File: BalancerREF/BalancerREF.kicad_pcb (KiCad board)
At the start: 4 copper layers, 50 x 50 mm, 79 parts, among them J1 USB4105-GF-A, J2 LiPo 500mAh PROTECTED, J3 MAG+ / MAG- PTH, J4 GPS MODULE 3V3 UART, J5 OPTICAL HEAD 7-WAY, Q4 AO3401A, SW1 POWER, SW2 ACQUIRE, SW3 BOOT / SERVICE, U1 ESP32-S3-MINI-1-N8, U10 SN74LVC1G123DCTR, U2 IIS3DWBTR, U3 LM1815MX/NOPB, U5 BQ24075RGT, U6 TPS63031DSKR, U7 SRV05-4MR6T1G, U9 SN74LVC1G132DBVR

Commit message: fix: BOM fields, silkscreen labels, +3V3 plane, and stale docs before review
- MPN fields: R3/R35/R36 (were "100k"), U9 (was the 1G08), R18 (was 3R0)
- Title block: HOBOVibe spelling; head company line no longer says "human
  review required"
- C20 on the head board rated 10 V; SYS_SW can sit at 5.5 V
- Silkscreen: board name and rev on both boards, battery and MAG polarity,
  pin-1 marks on J4 and both J5
- Main PCB: SYS, SYS_SW, BAT and USB_VBUS tracks removed from In2.Cu so the
  +3V3 plane is whole; three vias that only served them removed. Those four
  nets need re-routing on the outer layers.
- Docs: routing state, ground-pour wording, missing head-board holes,
  JLCPCB parts table rebuilt for the Rev F BOM, superseded LIS2DW12 and
  phototransistor sections marked in DATASHEET-VERIFICATION

Not done here (no KiCad in this environment): re-export of PDF/netlist/ERC/DRC.

Co-Authored-By: Claude Fable 5.1 <noreply@anthropic.com>
Claude-Session: https://claude.ai/code/session_01JeUyuyqf13Zf6V8TjfofPH
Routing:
- net /SYS_SW: track 54.6 -> 19.9 mm, vias 5 -> 4
- net /USB_VBUS: track 42.3 -> 8.03 mm, vias 5 -> 3
- net /BAT: track 25.1 -> 12.0 mm
- net /SYS: track 10.2 -> 2.68 mm
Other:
- board text added: "+"
- board text added: "-"
- board text added: "1"
- board text added: "HOBOVibe RevF"

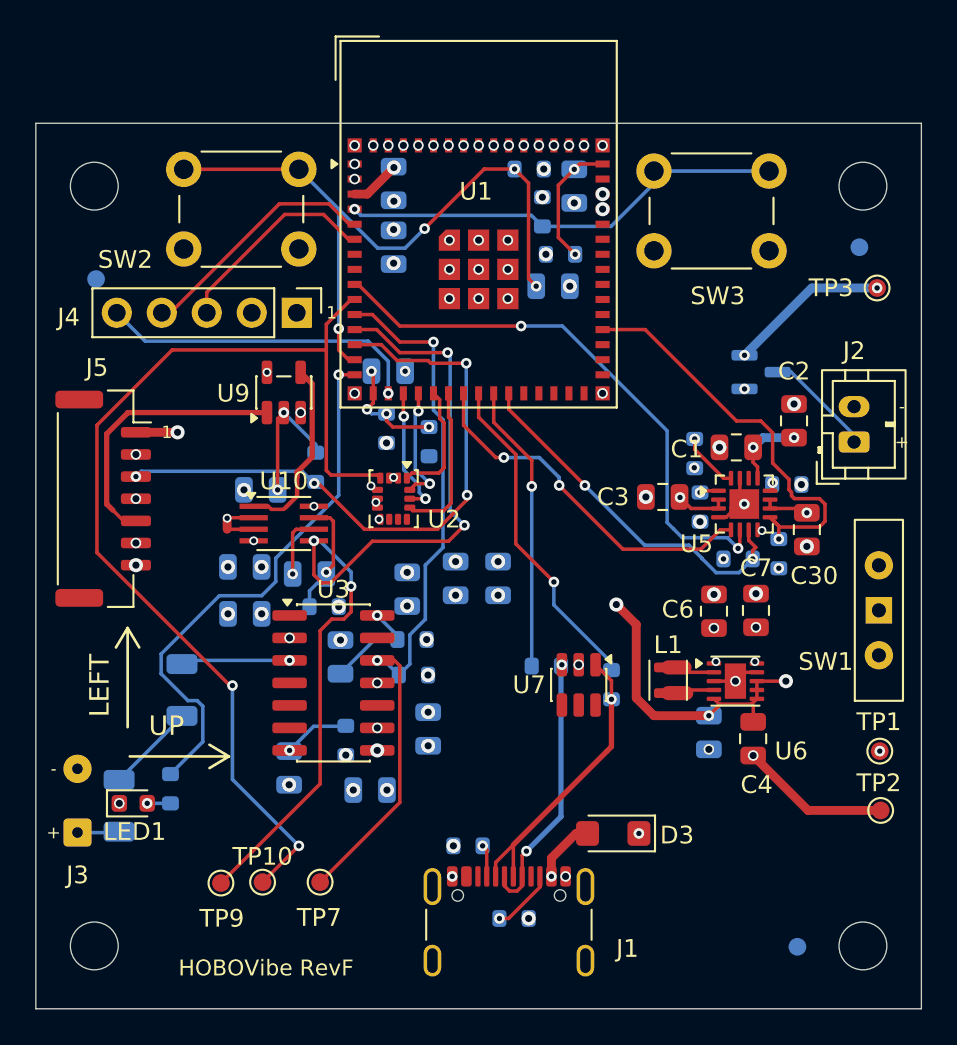
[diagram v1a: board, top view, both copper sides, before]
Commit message: feat: BalancerREF routed to a clean DRC
Power routing moved off the inner layers so In1 (GND) and In2 (+3V3) are
uncut planes. Thermal vias under the BQ24075 and TPS63031 exposed pads
(4 and 5). Switcher caps tight to the pins: C4 1.8 mm from VIN, C5 1.8 mm
from VINA, C6/C7 1.3 and 2.4 mm from VOUT; U2 decoupling within 1.6 mm.
SYS_SW bridged across U6 so VIN and VINA share one feed. Autorouter vias
resized to class values, stacked vias removed, silk polarity marks raised
to the minimum text height.

DRC: 0 errors, 0 unconnected. Remaining warnings are the GCT USB-C
footprint's own peg-to-pad spacing, the ESP32 module's antenna overhang,
and the local U1 footprint edit.

Rules: neck-down constraints now apply to F.Cu only (they were flagging
back-side tracks under front parts), U10 moved to the 0.65 mm group, and
the max-width clause dropped so the 0.5 mm cap feed may pass through U6's
courtyard.

Co-Authored-By: Claude Fable 5.1 <noreply@anthropic.com>
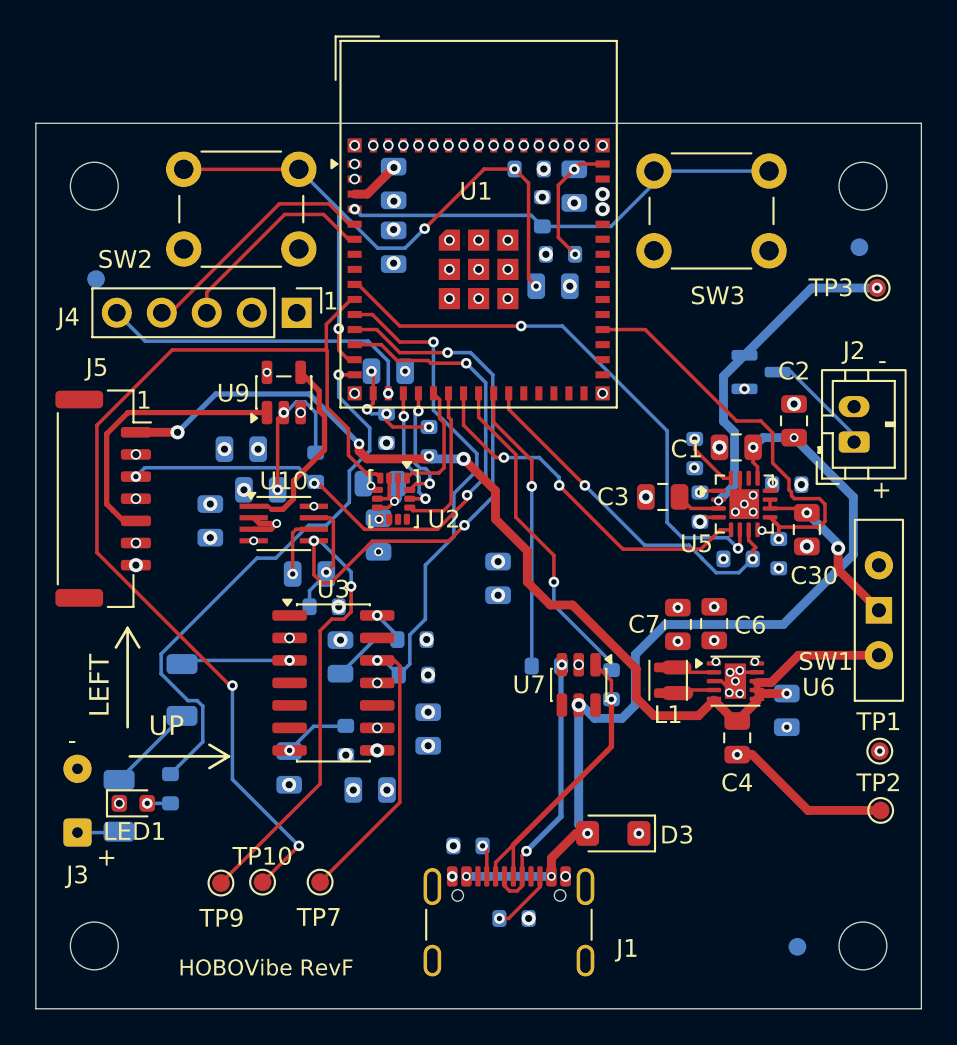
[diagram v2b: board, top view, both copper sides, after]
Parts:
- moved C13 6.83 mm to (119.5, 120.3), turned to 0 degrees
- moved C27 6.65 mm to (111.6, 118.4)
- moved C29 5.60 mm to (109.8, 122.5), turned to -90 degrees
- moved C5 4.57 mm to (142.4, 133.2)
- moved C7 4.48 mm to (136.2, 128.3), turned to 90 degrees
- moved C14 3.46 mm to (119.3, 123.2)
- moved C4 0.90 mm to (139.6, 134.7)
- moved C6 0.70 mm to (138.3, 128.2), turned to 90 degrees
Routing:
- net /USB_VBUS: track 8.03 -> 49.6 mm, vias 3 -> 6
- net /SYS_SW: track 19.9 -> 57.5 mm, vias 4 -> 5
- net /BAT: track 12.0 -> 21.4 mm, vias 3 -> 2
- net /SYS: track 2.68 -> 9.87 mm, vias 1 -> 2
- net GND: track 14.7 -> 20.5 mm, vias 81 -> 86
- net /OPT_TACH: track 51.7 -> 53.8 mm
- net /MAG_TACH: track 42.2 -> 43.8 mm
- net Net-(C26-Pad1): track 7.52 -> 9.07 mm
- net /STATUS_LED: track 31.0 -> 32.3 mm
- net /ACCEL_DRDY: track 59.8 -> 58.6 mm
- net /OPT_LED_EN: track 35.3 -> 36.1 mm
- net Net-(U10-~{A}): track 10.4 -> 11.0 mm
- net /+3V3: track 6.47 -> 6.16 mm, vias 29 -> 27

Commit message: fix: D3 polarity, U9 input bias, USB pair through U7
D3 SMF5.0A was drawn anode-to-VBUS. It is the unidirectional part of the
SMF family, so that is a forward diode across the USB supply - the board
would have collapsed VBUS and tripped the host port rather than
enumerating. Symbol rotated 180 degrees; the footprint turned with it and
the two pad nets swapped, so no track moved and the silkscreen band now
marks the VBUS end.

R39 and R40 (100k) pull U9's two Schmitt inputs low. Pin 1 floats whenever
the optical head is unplugged from J5 - normal for MR-VERT - and pin 2
while GPIO13 is still high-Z through the ESP32 boot. Low is the fail-safe
direction: the NAND holds Y high and U10's ~A trigger never falls.

U7's IO3 and IO4 join IO2 and IO1 on the two data nets, putting a second
pad of each net directly across the package, and U7 moved under the
connector ahead of R6/R7. Each USB line now enters one pad and leaves the
pad opposite instead of spurring off the series resistors' pads. Connector
pads to clamp pads: 11.95 mm before, 3.19 mm after.

DRC 7 violations, all pre-existing footprint issues, and 0 unconnected -
down from 10. ERC 0 errors. scripts/verify_netlist.py passes.

Co-Authored-By: Claude Opus 5 <noreply@anthropic.com>
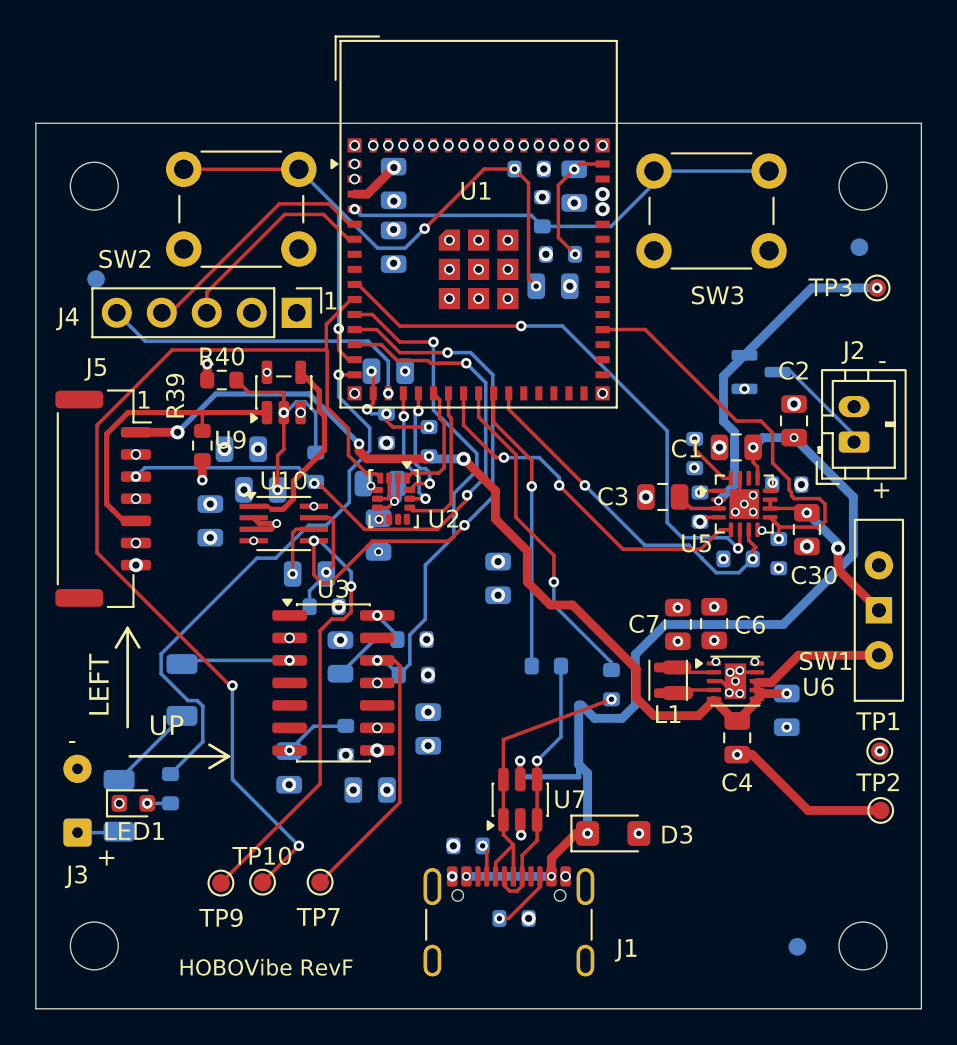
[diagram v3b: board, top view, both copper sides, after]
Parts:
- added R39: 100k, Resistor_SMD:R_0603_1608Metric, F.Cu at (109.4, 118.2)
- added R40: 100k, Resistor_SMD:R_0603_1608Metric, F.Cu at (110.5, 114.5)
- moved U7 7.28 mm to (127.3, 138.2), turned to 90 degrees
- turned D3 to 0 degrees
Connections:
- D3 pad 1: GND -> /USB_VBUS
- D3 pad 2: /USB_VBUS -> GND
- U7 pad 4: unconnected-(U7-IO3-Pad4) -> /USB_CONN_D+
- U7 pad 6: unconnected-(U7-IO4-Pad6) -> /USB_CONN_D-
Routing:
- net /USB_VBUS: track 49.6 -> 55.6 mm
- net Net-(C26-Pad1): track 9.07 -> 13.2 mm
- net GND: track 20.5 -> 23.4 mm, vias 86 -> 88
- net /OPT_COMP: track 15.6 -> 16.6 mm
- net /USB_CONN_D+: vias 2 -> 1
